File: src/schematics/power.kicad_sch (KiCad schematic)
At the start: 38 parts, among them U1 TPS565242DRDR, U2 TPS562202DRLR, U3 TPS562202DRLR, U4 TPS562202DRLR, U5 LM3880MF*-1AA

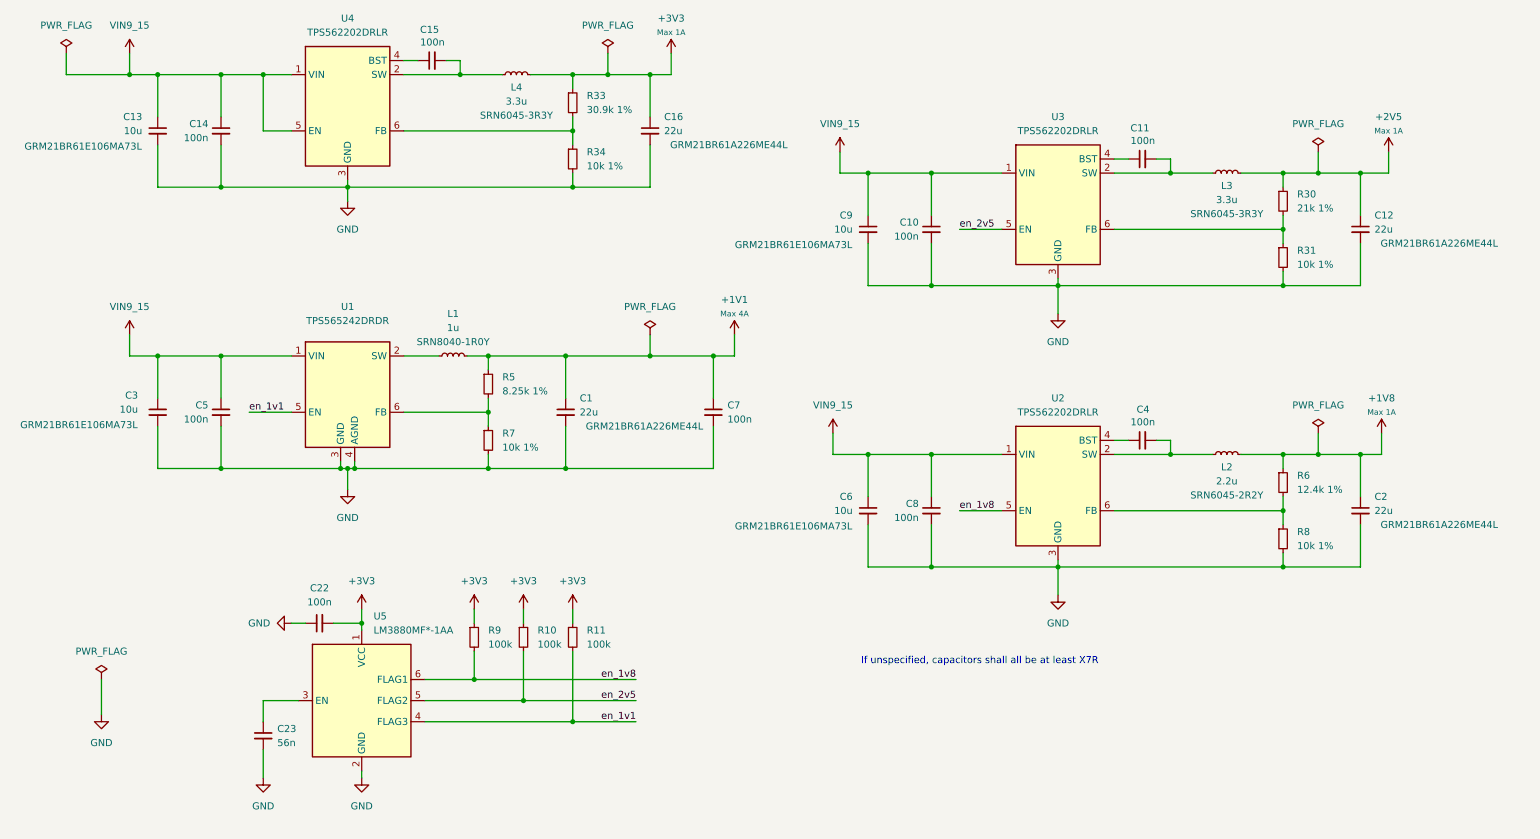
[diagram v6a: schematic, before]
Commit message: Add notes on the schematic
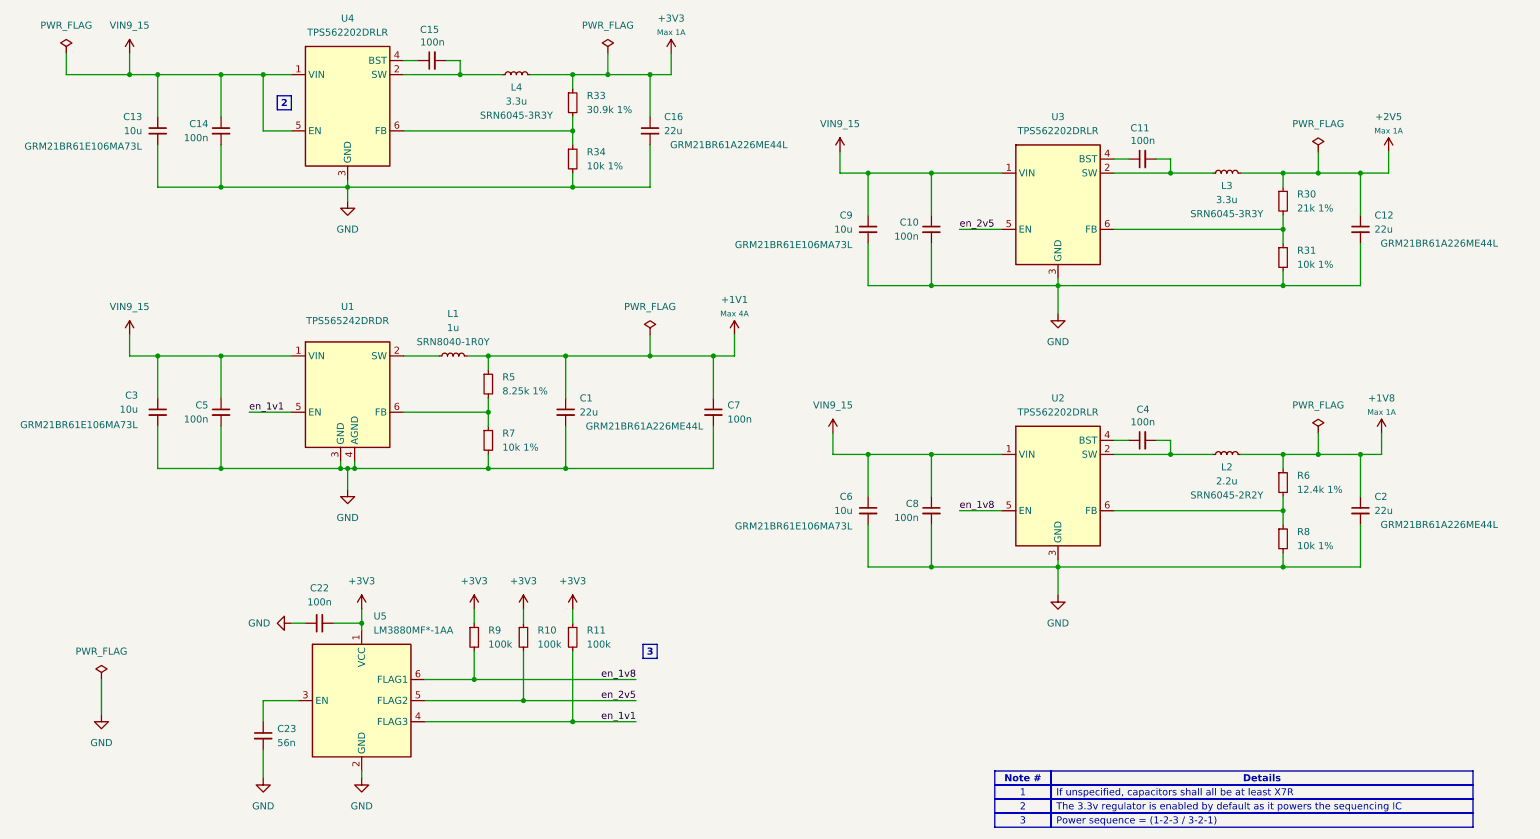
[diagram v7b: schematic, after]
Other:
- note removed: "If unspecified, capacitors shall all be at least X7R"
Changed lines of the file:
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@@
 		(comment 3 "${Part Number}")
 	)
-	(text "If unspecified, capacitors shall all be at least X7R"
-		(exclude_from_sim no)
-		(at 168.91 140.208 0)
-		(effects
-			(font
-				(size 1.27 1.27)
+	(text_box "Power sequence = (1-2-3 / 3-2-1)"
+		(exclude_from_sim no)
+		(at 203.2 167.64 0)
+		(size 76.2 2.54)
+		(margins 0.9525 0.9525 0.9525 0.9525)
+		(stroke
+			(width 0)
+			(type solid)
+			(color 0 0 0 1)
+		)
+		(fill
+			(type none)
+		)
+		(effects
+			(font
+				(face "Arial")
+				(size 1.27 1.27)
+				(color 0 0 0 1)
 			)
 			(justify left)
+		)
+	)
+	(text_box "3"
+		(exclude_from_sim no)
+		(at 193.04 167.64 0)
+		(size 10.16 2.54)
+		(margins 0.9525 0.9525 0.9525 0.9525)
+		(stroke
+			(width 0)
+			(type solid)
+			(color 0 0 0 1)
+		)
+		(fill
+			(type none)
+		)
+		(effects
+			(font
+				(face "Arial")
+				(size 1.27 1.27)
+				(color 0 0 0 1)
+			)
+		)
+	)
+	(text_box "2"
+		(exclude_from_sim no)
+		(at 193.04 165.1 0)
+		(size 10.16 2.54)
+		(margins 0.9525 0.9525 0.9525 0.9525)
+		(stroke
+			(width 0)
+			(type solid)
+			(color 0 0 0 1)
+		)
+		(fill
+			(type none)
+		)
+		(effects
+			(font
+				(face "Arial")
+				(size 1.27 1.27)
+				(color 0 0 0 1)
+			)
+		)
+	)
+	(text_box "2"
+		(exclude_from_sim no)
+		(at 63.5 38.1 0)
+		(size 2.54 2.54)
+		(margins 0.9525 0.9525 0.9525 0.9525)
+		(stroke
+			(width 0)
+			(type solid)
+			(color 0 0 0 1)
+		)
+		(fill
+			(type none)
+		)
+		(effects
+			(font
+				(face "Arial")
+				(size 1.27 1.27)
+				(bold yes)
+				(color 0 0 0 1)
+			)
+		)
+	)
+	(text_box "3"
+		(exclude_from_sim no)
+		(at 129.54 137.16 0)
+		(size 2.54 2.54)
+		(margins 0.9525 0.9525 0.9525 0.9525)
+		(stroke
+			(width 0)
+			(type solid)
+			(color 0 0 0 1)
+		)
+		(fill
+			(type none)
+		)
+		(effects
+			(font
+				(face "Arial")
+				(size 1.27 1.27)
+				(bold yes)
+				(color 0 0 0 1)
+			)
+		)
+	)
+	(text_box "Details"
+		(exclude_from_sim no)
+		(at 203.2 160.02 0)
+		(size 76.2 2.54)
+		(margins 0.9525 0.9525 0.9525 0.9525)
+		(stroke
+			(width 0)
+			(type solid)
+			(color 0 0 0 1)
+		)
+		(fill
+			(type none)
+		)
+		(effects
+			(font
+				(face "Arial")
+				(size 1.27 1.27)
+				(bold yes)
+				(color 0 0 0 1)
+			)
+		)
+	)
+	(text_box "1"
+		(exclude_from_sim no)
+		(at 193.04 162.56 0)
+		(size 10.16 2.54)
+		(margins 0.9525 0.9525 0.9525 0.9525)
+		(stroke
+			(width 0)
+			(type solid)
+			(color 0 0 0 1)
+		)
+		(fill
+			(type none)
+		)
+		(effects
+			(font
+				(face "Arial")
+				(size 1.27 1.27)
+				(color 0 0 0 1)
+			)
+		)
+	)
+	(text_box "The 3.3v regulator is enabled by default as it powers the sequencing IC"
+		(exclude_from_sim no)
+		(at 203.2 165.1 0)
+		(size 76.2 2.54)
+		(margins 0.9525 0.9525 0.9525 0.9525)
+		(stroke
+			(width 0)
+			(type solid)
+			(color 0 0 0 1)
+		)
+		(fill
+			(type none)
+		)
+		(effects
+			(font
+				(face "Arial")
+				(size 1.27 1.27)
+				(color 0 0 0 1)
+			)
+			(justify left)
+		)
+	)
+	(text_box "Note #"
+		(exclude_from_sim no)
+		(at 193.04 160.02 0)
+		(size 10.16 2.54)
+		(margins 0.9525 0.9525 0.9525 0.9525)
+		(stroke
+			(width 0)
+			(type solid)
+			(color 0 0 0 1)
+		)
+		(fill
+			(type none)
+		)
+		(effects
+			(font
+				(face "Arial")
+				(size 1.27 1.27)
+				(bold yes)
+				(color 0 0 0 1)
+			)
+		)
+	)
+	(text_box "If unspecified, capacitors shall all be at least X7R"
+		(exclude_from_sim no)
+		(at 203.2 162.56 0)
+		(size 76.2 2.54)
+		(margins 0.9525 0.9525 0.9525 0.9525)
+		(stroke
+			(width 0)
+			(type solid)
+			(color 0 0 0 1)
+		)
+		(fill
+			(type none)
+		)
+		(effects
+			(font
+				(face "Arial")
+				(size 1.27 1.27)
+				(color 0 0 0 1)
+			)
+			(justify left)

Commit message: Route the board power supply (#89)
* Replaces the inductors for smaller ones

* Starts routing the power supply

* Starts routing power

* Start adding power planes

* Adds decoupling capacitors

* Adds routing of the power sequencing

* Add routing for SRAM

* Route the SRAM data pins

* Finish routing the SRAM

* Route the SDRAM

* Move 1.8v converter to other side of the board

* Start routing DDR2 data lanes

* Use 0402 resistors instead of 0201 for emmc termination

* Route signals from DDR2 to FPGA bank

* Update routing of emmc

* Route the DDR2 without length matching

* Add length matching for DDR on L4 and L6. Todo L1 and redo L6

* Update routing of DDR2 L6 traces. Todo L1

* Finish routing of ddr2 traces

* Update power layer to support stripline for ddr2

* Fixed mechanical holes
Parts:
- L1: footprint ECAP5-DPROC:Bourns_SRN8040 -> ECAP5-DPROC:Coilcraft_XAL4020
- L2: footprint ECAP5-DPROC:Bourns_SRN6045 -> ECAP5-DPROC:Coilcraft_XAL4020
- L3, L4: footprint ECAP5-DPROC:Bourns_SRN6045 -> ECAP5-DPROC:Coilcraft_XAL4030
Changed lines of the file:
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@@
 			)
 		)
-		(property "Footprint" "ECAP5-DPROC:Bourns_SRN8040"
+		(property "Footprint" "ECAP5-DPROC:Coilcraft_XAL4020"
 			(at 95.25 85.09 0)
 			(effects
@@
 		)
 		(instances
-			(project ""
+			(project "ecap5-bsom"
 				(path "/c5fd18a3-9aa0-4151-b6e0-94da3d606686/75c84b0f-c428-4bdf-a9d0-2de4281daa69"
 					(reference "L1")
@@
 		)
 		(instances
-			(project ""
+			(project "ecap5-bsom"
 				(path "/c5fd18a3-9aa0-4151-b6e0-94da3d606686/75c84b0f-c428-4bdf-a9d0-2de4281daa69"
 					(reference "U2")
@@
 		(on_board yes)
 		(dnp no)
-		(fields_autoplaced yes)
 		(property "Reference" "U1"
 			(at 76.2 76.2 0)
@@
 		)
 		(instances
-			(project ""
+			(project "ecap5-bsom"
 				(path "/c5fd18a3-9aa0-4151-b6e0-94da3d606686/75c84b0f-c428-4bdf-a9d0-2de4281daa69"
 					(reference "U1")
@@
 			)
 		)
-		(property "Footprint" "ECAP5-DPROC:Bourns_SRN6045"
+		(property "Footprint" "ECAP5-DPROC:Coilcraft_XAL4030"
 			(at 106.68 34.29 0)
 			(effects
@@
 		)
 		(instances
-			(project ""
+			(project "ecap5-bsom"
 				(path "/c5fd18a3-9aa0-4151-b6e0-94da3d606686/75c84b0f-c428-4bdf-a9d0-2de4281daa69"
 					(reference "C1")
@@
 			)
 		)
-		(property "Footprint" "ECAP5-DPROC:Bourns_SRN6045"
+		(property "Footprint" "ECAP5-DPROC:Coilcraft_XAL4030"
 			(at 234.95 52.07 0)
 			(effects
@@
 			)
 		)
-		(property "Footprint" "ECAP5-DPROC:Bourns_SRN6045"
+		(property "Footprint" "ECAP5-DPROC:Coilcraft_XAL4020"
 			(at 234.95 102.87 0)
 			(effects
